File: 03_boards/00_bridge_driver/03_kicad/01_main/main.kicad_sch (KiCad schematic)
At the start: 0 parts

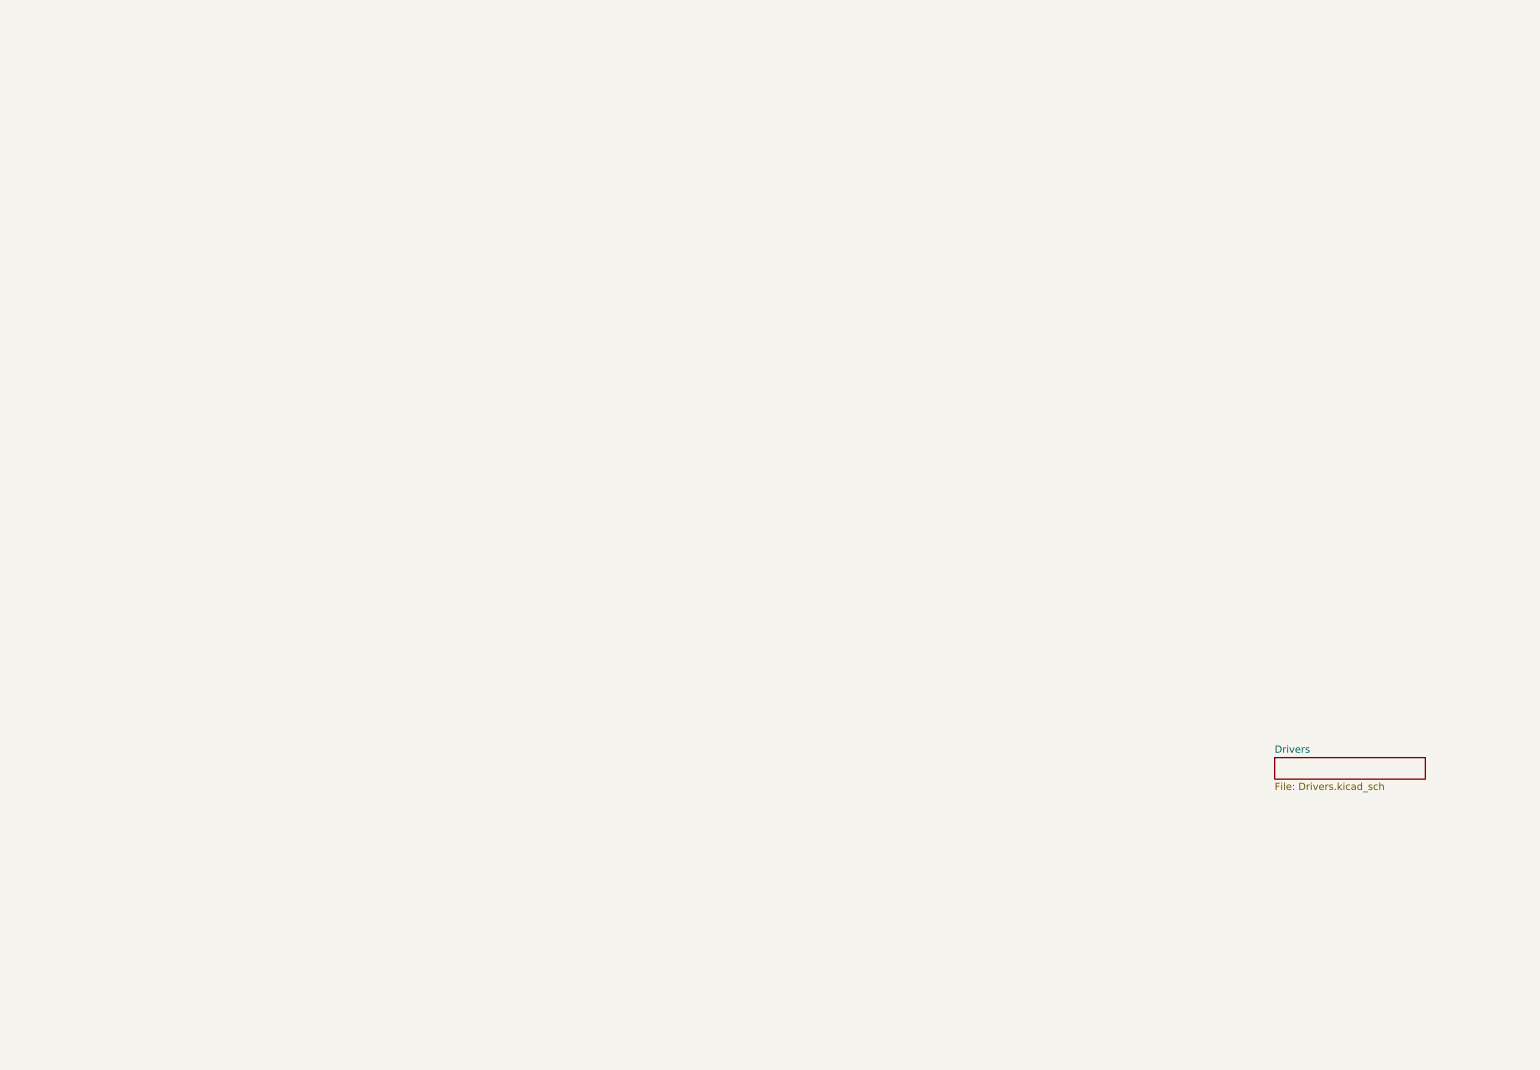
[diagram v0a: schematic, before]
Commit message: Week 0x7 | Streamlining deliverables (#31)
* Updated links and added note to BOM

* Fixed links

* Triple bridge driver layout

* Updated the readmes a bit and moved the analytical to 00_analytical

* Added notes about revision 3

* Added note about quality of the images

* Noted that prototype beta revision 2 is specifically not for fabrication.

* Added a note about revision 3

* Added break line

* Moved contributors and credits to /04_docs and also updated > sections

* Restructured the simulation section and simplified deliverables

* Improved documentation section at the bottom of the readme and improved 04_docs

* Updated readme.md

* Removed note.

* Fixed error with boards readme.md

* Added note about images requiring updates

* Add images to the readmes of a few sections

* Fixed point for new objective entry
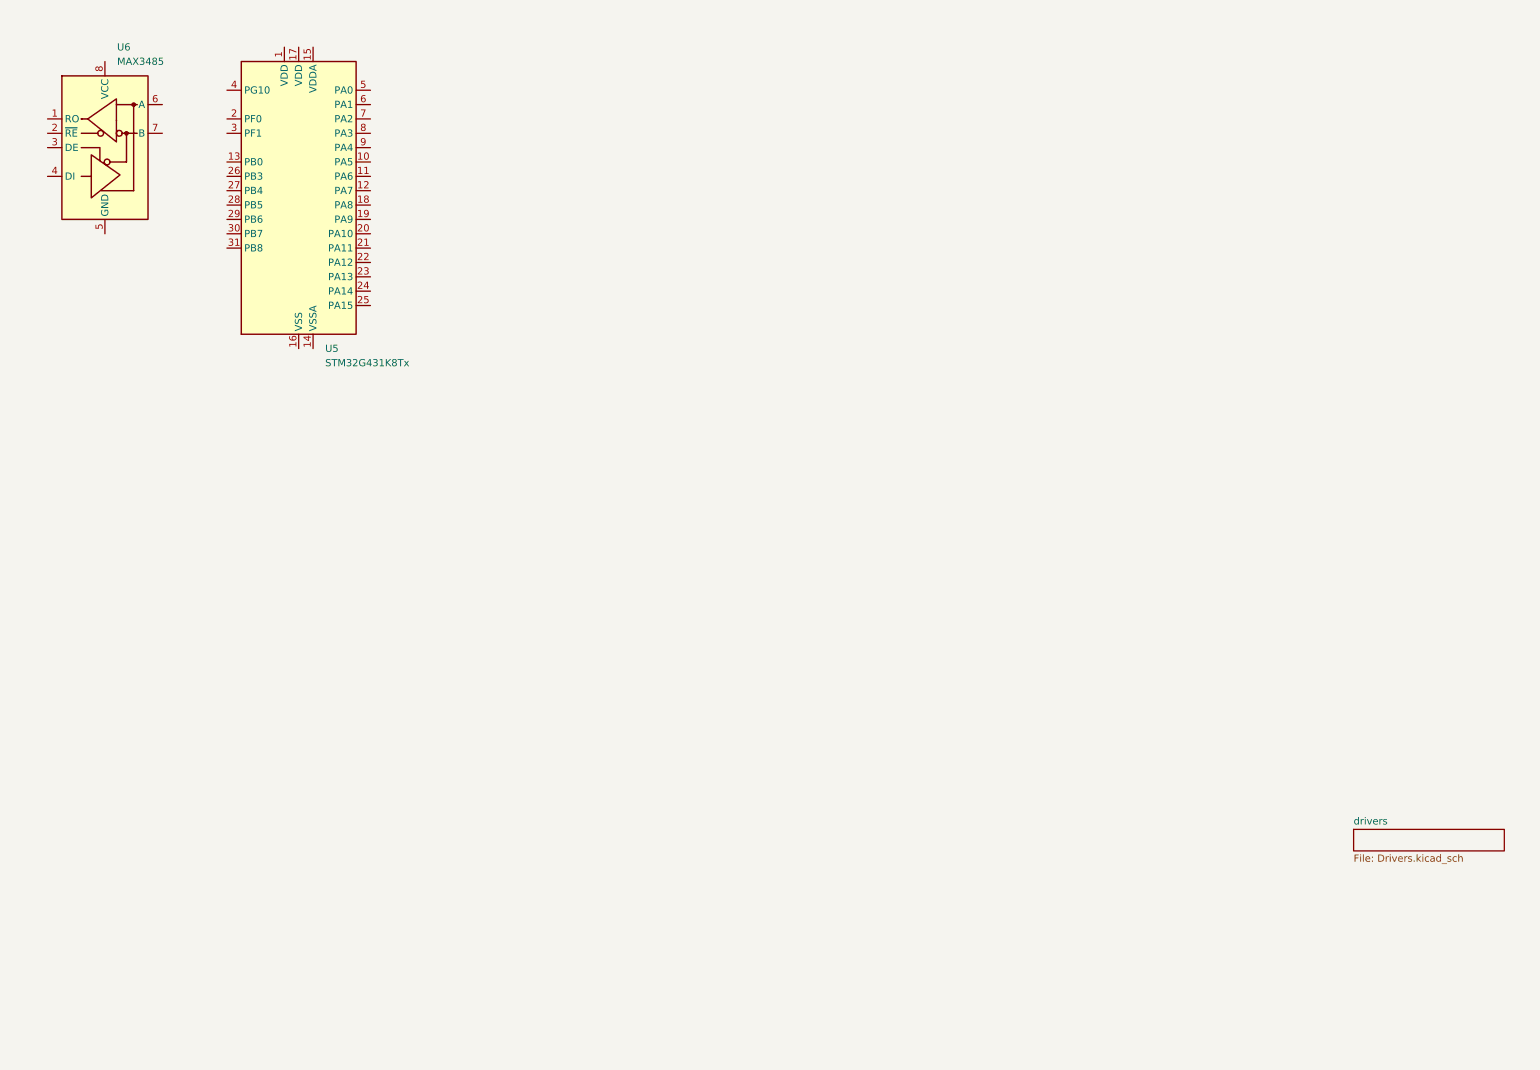
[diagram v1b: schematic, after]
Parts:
- added U5: STM32G431K8Tx, Package_QFP:LQFP-32_7x7mm_P0.8mm, symbol MCU_ST_STM32G4:STM32G431K8Tx
- added U6: MAX3485, Package_SO:SOIC-8_3.9x4.9mm_P1.27mm, symbol Interface_UART:MAX3485
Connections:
- new net: U5.16 (VSS), U5.32 (VSS)
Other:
- sheet Drivers renamed drivers
- title: Triple Bridge Driver -> Bridge Driver

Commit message: Week 0x8 | Simulation & Objectives (#34)
* Reordered motor folder and rewrote / cleaned up readmes within motors, boards and simulations

* Updated readme logo size

* Made logo 100% width

* Update scaled logo and removed finite element from readme

* Removed objectives

* Removed FEM from readme

* Removed Methodology

* Added a line break before prototype alpha image. Also removed figure naming from the document

* Trying a new formatting technique

* Moved boards link below image

* Removed `REV 2` from image description as its not needed

* Removing overview to see if its good or not

* Trying a new formatting style

* Removed the top line section

* Removed prototype from naming schema

* Changed top block

* Updated shields and updated description

* Removed some pose & added alpha and beta symbols because their cool

* Added a line break below documentation

* Added objectives to readme

* Removed the indexing from two notes

* Renamed `motor notes` with `alpha notes`

* Indexed the conceptual and removed : from note

* Updated parameter files and added short note about analytical model

* Cleaned up analytical model

* Updated analytical simulation

* Updated readmes for analytical model

* Updated the electrical equations

* Updated formatting for motors & boards

* Updated readmes and added sections to openLSM main readme

* I like it as a code block more

* Objectives should be in overview

* Moved aspirations note below objectives

* Made it more broad to contents than designs and contributions

* Updated subsection heading?

* Removed the "accurate dynamics" note its bad filler

* Removed TBD from readme

* Reformatting the tags section in documentation

* Updated analytical model

* Final iteration of analytical model before documentation

* Removing the global warning should be upto the individual readmes to say so

* Renamed metric.ut to derived.ut

* Added flow diagram for analytical model

* Updated the readmes to reflect uncertainty in the actual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
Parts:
- added C12, C13: 30pf, symbol Device:C
- added C14, C15, C17, C21: 100nf, symbol Device:C
- added C16, C19: 10uf, symbol Device:C
- added C18: 1uf, symbol Device:C
- added C20: 22uf, symbol Device:C
- added C22, C24: 680uF, symbol Device:C
- added C23, C25: 220uF, symbol Device:C
- added C26: 0.68uF, symbol Device:C
- added C27: 4.7uF, symbol Device:C
- added CAN1, J1, STEP1: 01x02, symbol Connector_Generic:Conn_01x02
- added D16: LED, symbol Device:LED
- added D17, D18: 1N5824, Diode_THT:D_DO-201AD_P15.24mm_Horizontal, symbol Diode:1N5822
- added FB1: BLM18AG601SN1D, symbol Device:FerriteBead
- added INT1: 01x04, symbol Connector_Generic:Conn_01x04
- added L1: 33uH, symbol Device:L
- added L2, L3: 68uH, symbol Device:L
- added L4: 10uH, symbol Device:L
- added PH1: 01x03, symbol Connector_Generic:Conn_01x03
- added PRO1: 01x06, symbol Connector_Generic:Conn_01x06
- added R11: 120, symbol Device:R
- added R12, R13: 10, symbol Device:R
- added R14, R15, R18: 220, symbol Device:R
- added R16, R17: 10K, symbol Device:R
- added SW1, SW2: SW_Push, symbol Switch:SW_Push
- added U14: CME0512S3C, CME_SC_MUR, symbol 2026-08-29_14-59-18:CME0512S3C
- added U15: CME0303S3C, CME_SC_MUR, symbol 2026-08-29_14-59-18:CME0512S3C
- added U7: LD1117V33, Package_TO_SOT_THT:TO-220-3_Vertical, symbol Regulator_Linear:LD1117V33
- added U8: LM2596S-5, Package_TO_SOT_SMD:TO-263-5_TabPin3, symbol Regulator_Switching:LM2596S-5
- added U9: LM2596S-12, Package_TO_SOT_SMD:TO-263-5_TabPin3, symbol Regulator_Switching:LM2596S-12
- added Y1: ECS-80-20-18-TR, ECS-80-20-18-TR:XTAL_ECS-80-20-18-TR, symbol ECS-80-20-18-TR:ECS-80-20-18-TR
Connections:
- net RS_RC: now reaches U6.1 (RO)
- net RS_RC: now also U5.27 (PB4), U5.28 (PB5)
- net RS_EN: now reaches U6.2 (~{RE})
- net RS_TOG: now reaches U6.3 (DE)
- net RS_TOG: now also U5.30 (PB7)
- net RS_DRI: now reaches U6.4 (DI)
- net RS_DRI: now also U5.29 (PB6)
- net GND: now reaches U6.5 (GND)
- net GND: now also U5.14 (VSSA), U5.16 (VSS), U5.32 (VSS), C12.2, C13.2, C14.2, C15.2, C16.2, C17.2, C18.2, C19.2, C20.2, C21.2, C22.2, C23.2, C24.2, C25.2, D16.1 (K), D17.2 (A), D18.2 (A), INT1.1 (Pin_1), J1.1 (Pin_1), PRO1.4 (Pin_4), R17.2, SW2.2, U14.1 (-VIN), U15.1 (-VIN), U7.1 (GND), U8.3 (GND), U8.5 (~{ON}/OFF), U9.3 (GND), U9.5 (~{ON}/OFF)
- net at U6.6 (A): now also R12.2
- net at U6.7 (B): now also R13.2
- net +3.3V: now reaches U6.8 (VCC)
- net +3.3V: now also C16.1, FB1.1, R14.1, U7.2 (VO)
- net VDDA: now reaches U5.1 (VDD)
- net VDDA: now also U5.15 (VDDA), U5.17 (VDD), C17.1, C18.1, C19.1, C20.1, FB1.2, R16.1
- net PHB_PWM: now reaches U5.10 (PA5)
- net +CAN: now reaches U5.12 (PA7)
- net +CAN: now also CAN1.2 (Pin_2)
- net DRI_ENA: now reaches U5.13 (PB0)
- net -CAN: now reaches U5.18 (PA8)
- net -CAN: now also CAN1.1 (Pin_1)
- net +STEP: now reaches U5.19 (PA9)
- net +STEP: now also STEP1.2 (Pin_2)
- net OSC_OUT: now reaches U5.2 (PF0)
- net OSC_OUT: now also C13.1, Y1.2, Y1.3
- net -STEP: now reaches U5.20 (PA10)
- net -STEP: now also STEP1.1 (Pin_1)
- net PHA_PWM: now reaches U5.21 (PA11)
- net at U5.22 (PA12): now also R18.1
- net SWDIO: now reaches U5.23 (PA13)
- net SWDIO: now also PRO1.3 (Pin_3)
- net SWCLK: now reaches U5.24 (PA14)
- net SWCLK: now also PRO1.5 (Pin_5)
- net PHC_PWM: now reaches U5.25 (PA15)
- net SWO: now reaches U5.26 (PB3)
- net SWO: now also PRO1.1 (Pin_1)
- net OSC_IN: now reaches U5.3 (PF1)
- net OSC_IN: now also C12.1, Y1.1, Y1.4
- net BOOT: now reaches U5.31 (PB8)
- net BOOT: now also C14.1, R17.1, SW1.2
- net NRST: now reaches U5.4 (PG10)
- net NRST: now also C15.1, PRO1.2 (Pin_2), R15.1, R16.2
- net CS1+: now reaches U5.6 (PA1)
- net CS1-: now reaches U5.7 (PA2)
- net CS2+: now reaches U5.8 (PA3)
- net CS2-: now reaches U5.9 (PA4)
- new net: L4.1, U15.4 (+VOUT)
- new net: D17.1 (K), L1.1, U8.2 (OUT)
- new net: R14.2, SW1.1
- new net: D16.2 (A), R18.2
- new net: R15.2, SW2.1
- new net: D18.1 (K), L2.1, U9.2 (OUT)
- new net: L3.1, U14.4 (+VOUT)
- new net +12V: C22.1, C25.1, L2.2, U15.2 (+VIN), U8.1 (VIN), U9.4 (FB)
- new net +12VIS: C27.1, L4.2
- new net +24V: C24.1, J1.2 (Pin_2), U9.1 (VIN)
- new net +3.3VIS: C26.1, L3.2
- new net +5V: C21.1, C23.1, INT1.4 (Pin_4), L1.2, PRO1.6 (Pin_6), U14.2 (+VIN), U7.3 (VI), U8.4 (FB)
- new net D_N: INT1.2 (Pin_2), INT1.3 (Pin_3), R11.2, R13.1
- new net D_P: R11.1, R12.1
- new net PA: PH1.3 (Pin_3)
- new net PB: PH1.2 (Pin_2)
- new net PC: PH1.1 (Pin_1)
- new net PGND: C26.2, C27.2, U14.3 (-VOUT), U15.3 (-VOUT)
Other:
- added sheet current (current.kicad_sch)
- note added: "3-Phase Interface"
- note added: "8 Mhz Oscillator"
- note added: "Boot / Reset"
- note added: "Control Interfaces"
- note added: "Controller (170 Mhz)"
- note added: "F, C"
- note added: "Isolated 12V Supply"
- note added: "Low dropout regulator (5V to 3.3V)"
- note added: "Power & Interconnect"
- note added: "Programming Interface"
- note added: "RS-485/RS-422 Terminations"
- note added: "RS-485/RS-422 Transceiver"
- note added: "Step down regulator (12V to 5V)"
- note added: "Step down regulator (24V to 12V)"
- note added: "VDDA Decoupling"
- note added: "WARNING: For current sensing, use either the `1 mΩ`, `3 mΩ`, or `10 mΩ` shunt resistor. Do not use more than a single path, or the driver will not function correctly."
- moved on the sheet: U5, U6

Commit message: More footprint selection. YAY
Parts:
- removed L4: 10uH, symbol Device:L
- added L5: 82103C, symbol 2026-09-06_15-58-36:82103C
- CAN1, STEP1: footprint (none) -> Connector_JST:JST_PH_B2B-PH-K_1x02_P2.00mm_Vertical
- D16: footprint (none) -> LED_SMD:LED_0603_1608Metric_Pad1.05x0.95mm_HandSolder
- FB1: footprint (none) -> BLM18AG601SN1D:BEADC1608X95N
- INT1: footprint (none) -> Connector_JST:JST_PH_B4B-PH-K_1x04_P2.00mm_Vertical
- PRO1: footprint (none) -> Connector_JST:JST_PH_B6B-PH-K_1x06_P2.00mm_Vertical
- R11, R12, R13, R14, R15, R16, R17, R18: footprint (none) -> Resistor_SMD:R_0603_1608Metric
- SW1, SW2: footprint (none) -> Button_Switch_SMD:SW_Push_1P1T_NO_CK_KMR2
- U14, U15: footprint CME_SC_MUR -> CME0512S3C:CME_SC_MUR
- Y1: footprint ECS-80-20-18-TR:XTAL_ECS-80-20-18-TR -> ECS-80-18-23B-JTN-TR:XTAL_ECS-80-20-18-TR
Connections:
- net +12VIS: now also L5.1
- net at U15.4 (+VOUT): now also L5.2
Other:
- note removed: "F, C"
- moved on the sheet: C27

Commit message: More footprints.
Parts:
- D17, D18: footprint Diode_THT:D_DO-201AD_P15.24mm_Horizontal -> Diode_SMD:D_SMC
- J1: footprint (none) -> Connector_Wire:SolderWire-1sqmm_1x02_P7.8mm_D1.4mm_OD3.9mm
- L3: value 68uH -> 82683C
- PH1: footprint (none) -> Connector_Wire:SolderWire-2.5sqmm_1x03_P7.2mm_D2.4mm_OD3.6mm_Relief
- U7: footprint Package_TO_SOT_THT:TO-220-3_Vertical -> Package_TO_SOT_SMD:SOT-223
- renumbered L5 to L4
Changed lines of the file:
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@@
 			)
 		)
-		(property "Footprint" ""
+		(property "Footprint" "Connector_Wire:SolderWire-2.5sqmm_1x03_P7.2mm_D2.4mm_OD3.6mm_Relief"
 			(at 20.32 162.56 0)
 			(hide yes)
@@
 			)
 		)
-		(property "Footprint" ""
+		(property "Footprint" "Connector_Wire:SolderWire-1sqmm_1x02_P7.8mm_D1.4mm_OD3.9mm"
 			(at 21.59 33.02 0)
 			(hide yes)
@@
 			)
 		)
-		(property "Footprint" "Package_TO_SOT_THT:TO-220-3_Vertical"
+		(property "Footprint" "Package_TO_SOT_SMD:SOT-223"
 			(at 82.55 99.06 0)
 			(hide yes)
@@
 			)
 		)
-		(property "Value" "68uH"
+		(property "Value" "82683C"
 			(at 114.554 144.272 90)
 			(show_name no)
@@
 		(dnp no)
 		(fields_autoplaced yes)
-		(property "Reference" "L5"
+		(property "Reference" "L4"
 			(at 114.3 168.91 0)
 			(show_name no)
@@
 			(project "main"
 				(path "/221b5544-ca14-4503-b001-a85fc346b8a9"
-					(reference "L5")
+					(reference "L4")
 					(unit 1)
 				)
@@
 			)
 		)
-		(property "Footprint" "Diode_THT:D_DO-201AD_P15.24mm_Horizontal"
+		(property "Footprint" "Diode_SMD:D_SMC"
 			(at 86.995 76.2 0)
 			(hide yes)
@@
 			)
 		)
-		(property "Footprint" "Diode_THT:D_DO-201AD_P15.24mm_Horizontal"
+		(property "Footprint" "Diode_SMD:D_SMC"
 			(at 86.995 39.37 0)
 			(hide yes)
